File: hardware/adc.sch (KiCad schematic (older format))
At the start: 2 parts

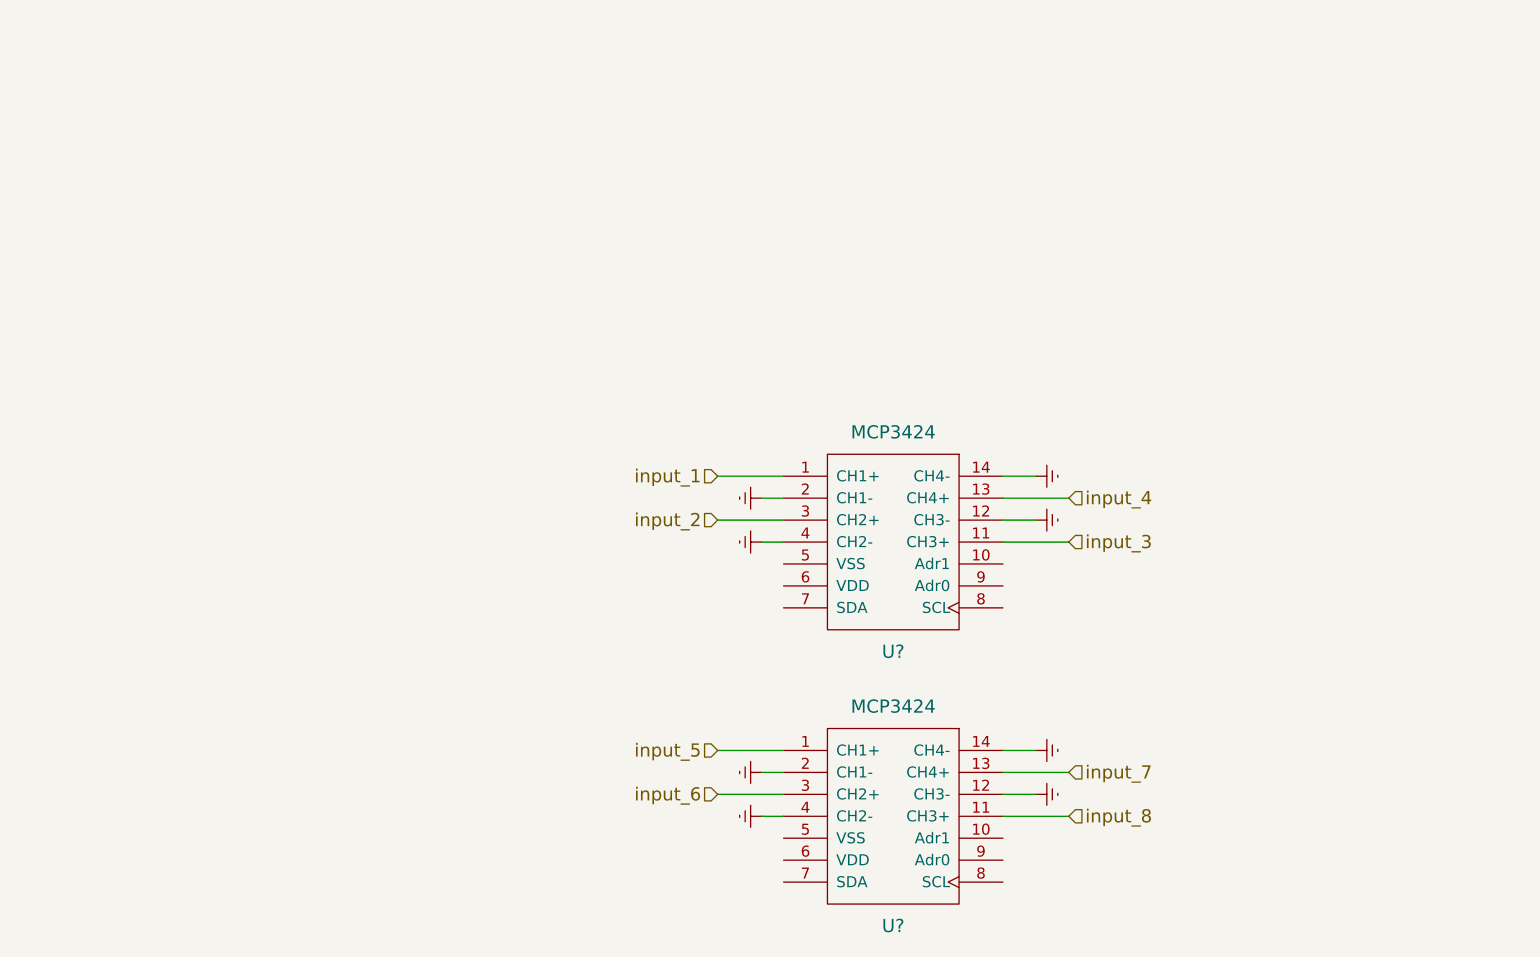
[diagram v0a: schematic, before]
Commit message: power added to second adc
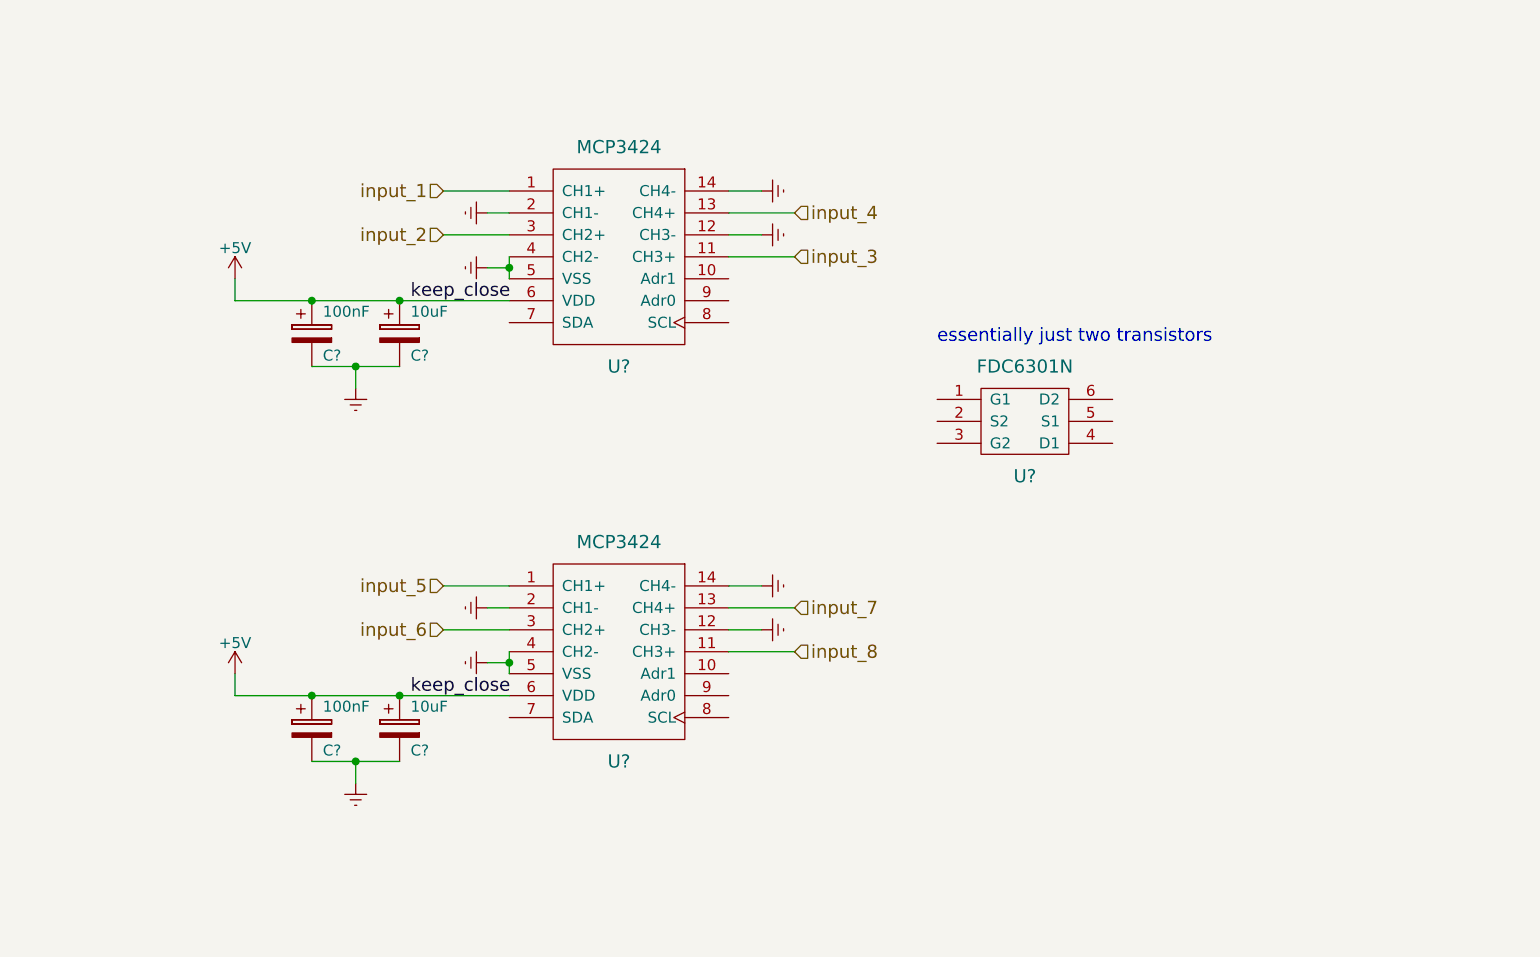
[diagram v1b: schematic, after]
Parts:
- added C? (x2): 10uF, symbol CP
- added C? (x2): 100nF, symbol CP
- added U?: FDC6301N, symbol FDC6301N
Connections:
- net Earth: now also U?.5 (VSS), U?.5 (VSS), C?.2, C?.2, C?.2, C?.2
- net +5V: now reaches U?.6 (VDD)
- net +5V: now also U?.6 (VDD), C?.1, C?.1, C?.1, C?.1
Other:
- note added: "essentially just two transistors"
- moved on the sheet: U?

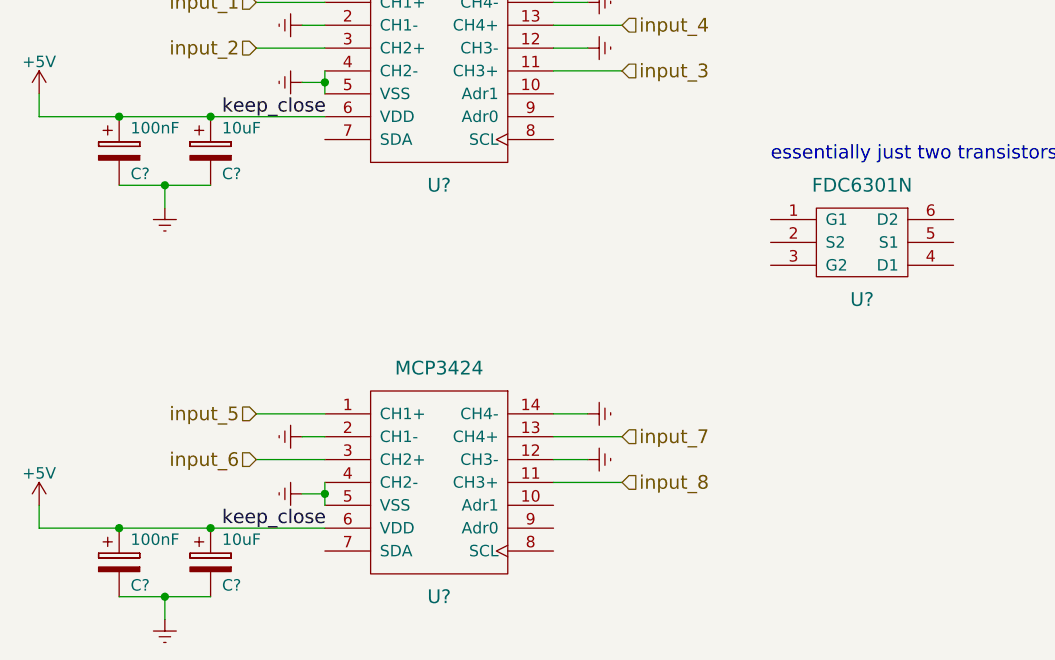
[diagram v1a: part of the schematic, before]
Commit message: jacks on a different sheet than the buffers. single PCB with jumpers and mouse bites
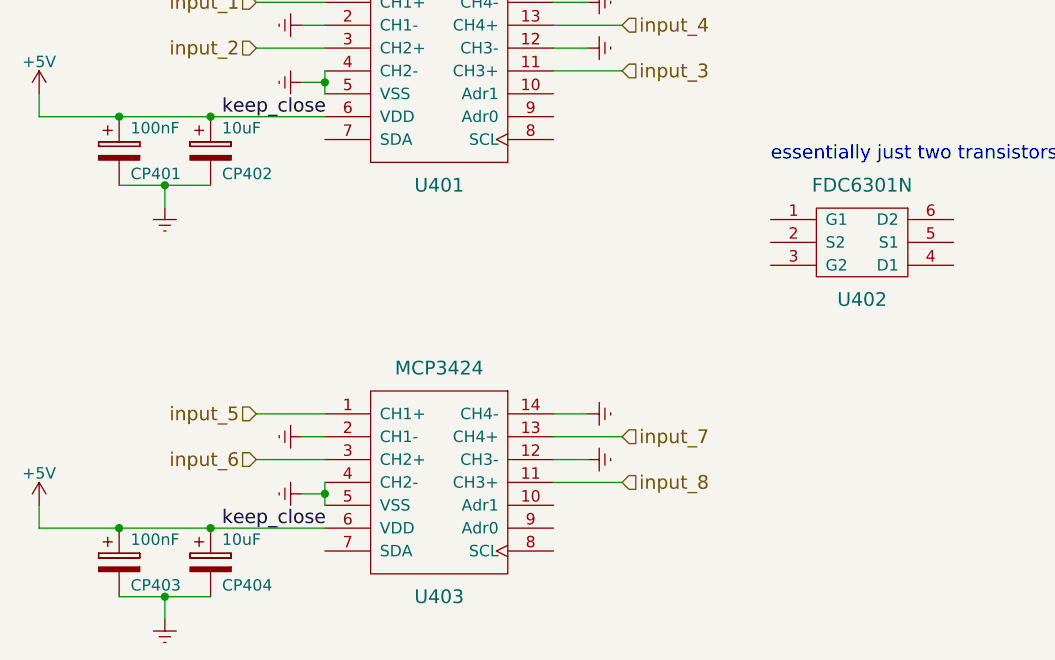
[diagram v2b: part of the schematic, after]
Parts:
- U401, U403: renamed from U?; footprint (none) -> Housings_SOIC:SOIC-14_3.9x8.7mm_Pitch1.27mm
- gave numbers to parts that had none: 5
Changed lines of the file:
@@
 $Descr A4 11693 8268
 encoding utf-8
-Sheet 4 4
+Sheet 4 6
 Title ""
 Date ""
@@
 input_8
 $Comp
-L MCP3424 U?
+L MCP3424 U401
 U 1 1 5BDF6151
 P 3650 1800
-F 0 "U?" H 3650 1300 60  0000 C CNN
+F 0 "U401" H 3650 1300 60  0000 C CNN
 F 1 "MCP3424" H 3650 2300 60  0000 C CNN
-F 2 "" H 3650 1800 60  0001 C CNN
+F 2 "Housings_SOIC:SOIC-14_3.9x8.7mm_Pitch1.27mm" H 3650 1800 60  0001 C CNN
 F 3 "" H 3650 1800 60  0001 C CNN
 	1    3650 1800
@@
 $EndComp
 $Comp
-L MCP3424 U?
+L MCP3424 U403
 U 1 1 5BDF618D
 P 3650 3600
-F 0 "U?" H 3650 3100 60  0000 C CNN
+F 0 "U403" H 3650 3100 60  0000 C CNN
 F 1 "MCP3424" H 3650 4100 60  0000 C CNN
-F 2 "" H 3650 3600 60  0001 C CNN
+F 2 "Housings_SOIC:SOIC-14_3.9x8.7mm_Pitch1.27mm" H 3650 3600 60  0001 C CNN
 F 3 "" H 3650 3600 60  0001 C CNN
 	1    3650 3600
@@
 	4450 1600 4150 1600
 $Comp
-L Earth #PWR?
+L Earth #PWR033
 U 1 1 5BE328ED
 P 3050 1600
-F 0 "#PWR?" H 3050 1350 50  0001 C CNN
+F 0 "#PWR033" H 3050 1350 50  0001 C CNN
 F 1 "Earth" H 3050 1450 50  0001 C CNN
 F 2 "" H 3050 1600 50  0000 C CNN
@@
 	3050 1600 3150 1600
 $Comp
-L Earth #PWR?
+L Earth #PWR034
 U 1 1 5BE3290F
 P 3050 1850
-F 0 "#PWR?" H 3050 1600 50  0001 C CNN
+F 0 "#PWR034" H 3050 1600 50  0001 C CNN
 F 1 "Earth" H 3050 1700 50  0001 C CNN
 F 2 "" H 3050 1850 50  0000 C CNN
@@
 $EndComp
 $Comp
-L Earth #PWR?
+L Earth #PWR035
 U 1 1 5BE32932
 P 4300 1500
-F 0 "#PWR?" H 4300 1250 50  0001 C CNN
+F 0 "#PWR035" H 4300 1250 50  0001 C CNN
 F 1 "Earth" H 4300 1350 50  0001 C CNN
 F 2 "" H 4300 1500 50  0000 C CNN
@@
 	4300 1500 4150 1500
 $Comp
-L Earth #PWR?
+L Earth #PWR036
 U 1 1 5BE32956
 P 4300 1700
-F 0 "#PWR?" H 4300 1450 50  0001 C CNN
+F 0 "#PWR036" H 4300 1450 50  0001 C CNN
 F 1 "Earth" H 4300 1550 50  0001 C CNN
 F 2 "" H 4300 1700 50  0000 C CNN
@@
 	2850 3300 3150 3300
 $Comp
-L Earth #PWR?
+L Earth #PWR037
 U 1 1 5BE329E0
 P 4300 3500
-F 0 "#PWR?" H 4300 3250 50  0001 C CNN
+F 0 "#PWR037" H 4300 3250 50  0001 C CNN
 F 1 "Earth" H 4300 3350 50  0001 C CNN
 F 2 "" H 4300 3500 50  0000 C CNN
@@
 	4300 3500 4150 3500
 $Comp
-L Earth #PWR?
+L Earth #PWR038
 U 1 1 5BE32A0A
 P 4300 3300
-F 0 "#PWR?" H 4300 3050 50  0001 C CNN
+F 0 "#PWR038" H 4300 3050 50  0001 C CNN
 F 1 "Earth" H 4300 3150 50  0001 C CNN
 F 2 "" H 4300 3300 50  0000 C CNN
@@
 $EndComp
 $Comp
-L Earth #PWR?
+L Earth #PWR039
 U 1 1 5BE32A35
 P 3050 3400
-F 0 "#PWR?" H 3050 3150 50  0001 C CNN
+F 0 "#PWR039" H 3050 3150 50  0001 C CNN
 F 1 "Earth" H 3050 3250 50  0001 C CNN
 F 2 "" H 3050 3400 50  0000 C CNN
@@
 	3050 3400 3150 3400
 $Comp
-L Earth #PWR?
+L Earth #PWR040
 U 1 1 5BE32A71
 P 3050 3650
-F 0 "#PWR?" H 3050 3400 50  0001 C CNN
+F 0 "#PWR040" H 3050 3400 50  0001 C CNN
 F 1 "Earth" H 3050 3500 50  0001 C CNN
 F 2 "" H 3050 3650 50  0000 C CNN
@@
 	4300 3300 4150 3300
 $Comp
-L +5V #PWR?
+L +5V #PWR041
 U 1 1 5BE37FBA
 P 1900 1900
-F 0 "#PWR?" H 1900 1750 50  0001 C CNN
+F 0 "#PWR041" H 1900 1750 50  0001 C CNN
 F 1 "+5V" H 1900 2040 50  0000 C CNN
 F 2 "" H 1900 1900 50  0000 C CNN
@@
 $EndComp
 $Comp
-L Earth #PWR?
+L Earth #PWR042
 U 1 1 5BE38215
 P 2450 2400
-F 0 "#PWR?" H 2450 2150 50  0001 C CNN
+F 0 "#PWR042" H 2450 2150 50  0001 C CNN
 F 1 "Earth" H 2450 2250 50  0001 C CNN
 F 2 "" H 2450 2400 50  0000 C CNN
@@
 $EndComp
 $Comp
-L CP C?
+L CP CP402
 U 1 1 5BE3829F
 P 2650 2150
-F 0 "C?" H 2700 2050 50  0000 L CNN
+F 0 "CP402" H 2700 2050 50  0000 L CNN
 F 1 "10uF" H 2700 2250 50  0000 L CNN
-F 2 "" H 2688 2000 50  0000 C CNN
+F 2 "" H 2688 2000 50  0001 C CNN
 F 3 "" H 2650 2150 50  0000 C CNN
 	1    2650 2150
@@
 $EndComp
 $Comp
-L CP C?
+L CP CP401
 U 1 1 5BE382F8
 P 2250 2150
-F 0 "C?" H 2300 2050 50  0000 L CNN
+F 0 "CP401" H 2300 2050 50  0000 L CNN
 F 1 "100nF" H 2300 2250 50  0000 L CNN
-F 2 "" H 2288 2000 50  0000 C CNN
+F 2 "" H 2288 2000 50  0001 C CNN
 F 3 "" H 2250 2150 50  0000 C CNN
 	1    2250 2150
@@
 	1900 2000 1900 1900
 $Comp
-L FDC6301N U?
+L FDC6301N U402
 U 1 1 5BE3898B
 P 5500 2550
-F 0 "U?" H 5500 2300 60  0000 C CNN
+F 0 "U402" H 5500 2300 60  0000 C CNN
 F 1 "FDC6301N" H 5500 2800 60  0000 C CNN
 F 2 "" H 5350 2550 60  0001 C CNN
@@
 essentially just two transistors
 $Comp
-L Earth #PWR?
+L Earth #PWR043
 U 1 1 5BE44E1F
 P 2450 4200
-F 0 "#PWR?" H 2450 3950 50  0001 C CNN
+F 0 "#PWR043" H 2450 3950 50  0001 C CNN
 F 1 "Earth" H 2450 4050 50  0001 C CNN
 F 2 "" H 2450 4200 50  0000 C CNN
@@
 $EndComp
 $Comp
-L CP C?
+L CP CP404
 U 1 1 5BE44E25
 P 2650 3950
-F 0 "C?" H 2700 3850 50  0000 L CNN
+F 0 "CP404" H 2700 3850 50  0000 L CNN
 F 1 "10uF" H 2700 4050 50  0000 L CNN
-F 2 "" H 2688 3800 50  0000 C CNN
+F 2 "" H 2688 3800 50  0001 C CNN
 F 3 "" H 2650 3950 50  0000 C CNN
 	1    2650 3950
@@
 $EndComp
 $Comp
-L CP C?
+L CP CP403
 U 1 1 5BE44E2C
 P 2250 3950
-F 0 "C?" H 2300 3850 50  0000 L CNN
+F 0 "CP403" H 2300 3850 50  0000 L CNN
 F 1 "100nF" H 2300 4050 50  0000 L CNN
-F 2 "" H 2288 3800 50  0000 C CNN
+F 2 "" H 2288 3800 50  0001 C CNN
 F 3 "" H 2250 3950 50  0000 C CNN
 	1    2250 3950
@@
 Connection ~ 3150 3650
 $Comp
-L +5V #PWR?
+L +5V #PWR044
 U 1 1 5BE44ED3
 P 1900 3700
-F 0 "#PWR?" H 1900 3550 50  0001 C CNN
+F 0 "#PWR044" H 1900 3550 50  0001 C CNN
 F 1 "+5V" H 1900 3840 50  0000 C CNN
 F 2 "" H 1900 3700 50  0000 C CNN
